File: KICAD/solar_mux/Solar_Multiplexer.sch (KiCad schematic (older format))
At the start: 34 parts, among them J1 Conn_01x14, J2 Conn_02x06_Odd_Even, J3 Conn_02x06_Odd_Even, U1 ASSR-1611, U10 ASSR-1611, U11 ASSR-1611, U12 ASSR-1611, U13 ASSR-1611, U14 ASSR-1611, U15 ASSR-1611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

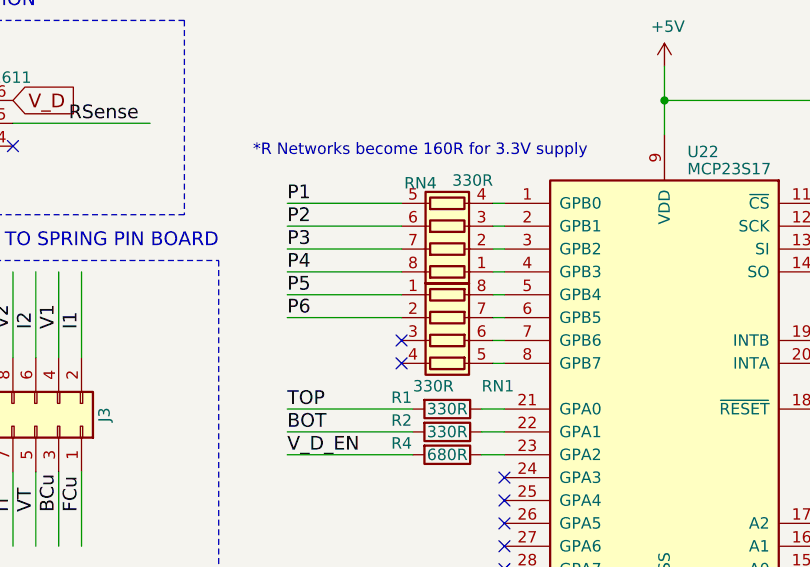
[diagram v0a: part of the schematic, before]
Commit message: Changing Via sizes and track widths
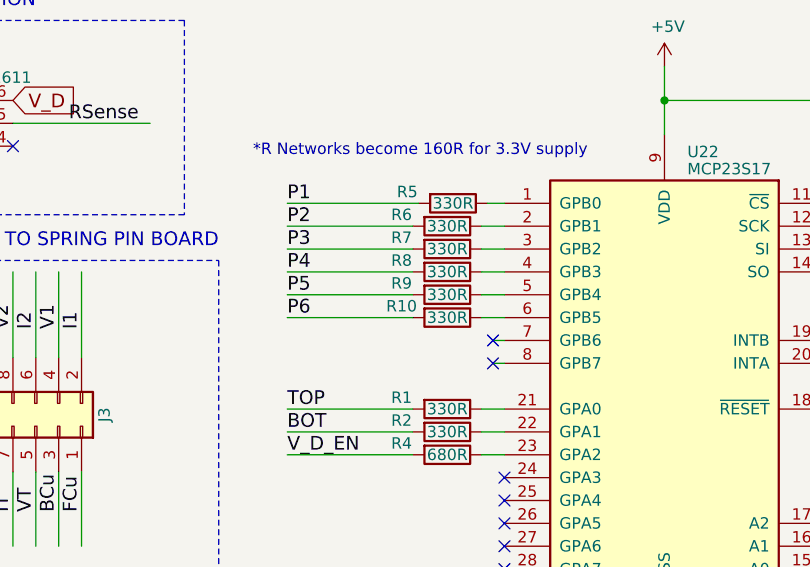
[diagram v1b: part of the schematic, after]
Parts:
- removed RN1, RN4: 330R, Resistor_SMD:R_Array_Convex_4x1206, symbol Device:R_Pack04
- added R10, R5, R6, R7, R8, R9: 330R, Resistor_THT:R_Axial_DIN0309_L9.0mm_D3.2mm_P15.24mm_Horizontal, symbol Device:R
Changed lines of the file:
@@
 	8500 2050 8450 2050
-Wire Wire Line
-	8500 1950 8450 1950
-Wire Wire Line
-	8500 1850 8450 1850
-Wire Wire Line
-	8500 1750 8450 1750
-Wire Wire Line
-	8500 1650 8450 1650
-Wire Wire Line
-	8500 1550 8450 1550
-Wire Wire Line
-	8500 1450 8450 1450
 Wire Wire Line
 	2150 1400 3750 1400
@@
 $EndComp
 $Comp
-L Device:R_Pack04 RN4
-U 1 1 5A00668D
-P 8250 1550
-F 0 "RN4" V 8438 1596 50  0000 L CNN
-F 1 "330R" V 8450 1350 50  0000 L CNN
-F 2 "Resistor_SMD:R_Array_Convex_4x1206" V 8525 1550 50  0001 C CNN
-F 3 "" H 8250 1550 50  0001 C CNN
-F 4 "744C083331JPCT-ND" H 8250 1550 60  0001 C CNN "digikey"
-	1    8250 1550
-	0    -1   -1   0
-$EndComp
-$Comp
 L Connector:TestPoint TP1
 U 1 1 5A007B84
@@
 	1    0    0    -1
 $EndComp
-$Comp
-L Device:R_Pack04 RN1
-U 1 1 5C453849
-P 8250 2050
-F 0 "RN1" V 8450 2200 50  0000 L CNN
-F 1 "330R" V 8450 1900 50  0000 L CNN
-F 2 "Resistor_SMD:R_Array_Convex_4x1206" V 8525 2050 50  0001 C CNN
-F 3 "" H 8250 2050 50  0001 C CNN
-F 4 "744C083331JPCT-ND" H 8250 2050 60  0001 C CNN "digikey"
-	1    8250 2050
-	0    1    1    0
-$EndComp
 Wire Wire Line
 	2200 4200 2150 4200
@@
 Text Label 6450 2000 1    60   ~ 0
 I2
-NoConn ~ 8050 2050
-NoConn ~ 8050 2150
+NoConn ~ 8450 2050
+NoConn ~ 8450 2150
 $Comp
 L power:+5V #PWR0107
@@
 	1    0    0    -1
 $EndComp
-Wire Wire Line
-	7550 1450 8050 1450
-Wire Wire Line
-	7550 1550 8050 1550
-Wire Wire Line
-	7550 1650 8050 1650
-Wire Wire Line
-	7550 1750 8050 1750
-Wire Wire Line
-	7550 1850 8050 1850
-Wire Wire Line
-	7550 1950 8050 1950
+$Comp
+L Device:R R5
+U 1 1 60480F1E
+P 8275 1450
+F 0 "R5" V 8225 1250 50  0000 C CNN
+F 1 "330R" V 8275 1450 50  0000 C CNN
+F 2 "Resistor_THT:R_Axial_DIN0309_L9.0mm_D3.2mm_P15.24mm_Horizontal" V 8205 1450 50  0001 C CNN
+F 3 "" H 8275 1450 50  0000 C CNN
+F 4 "2073607" H -2325 450 50  0001 C CNN "farnellCode"
+	1    8275 1450
+	0    1    1    0
+$EndComp
+Wire Wire Line
+	8425 1450 8500 1450
+Wire Wire Line
+	7550 1450 8125 1450
+$Comp
+L Device:R R6
+U 1 1 60492A33
+P 8250 1550
+F 0 "R6" V 8200 1350 50  0000 C CNN
+F 1 "330R" V 8250 1550 50  0000 C CNN
+F 2 "Resistor_THT:R_Axial_DIN0309_L9.0mm_D3.2mm_P15.24mm_Horizontal" V 8180 1550 50  0001 C CNN
+F 3 "" H 8250 1550 50  0000 C CNN
+F 4 "2073607" H -2350 550 50  0001 C CNN "farnellCode"
+	1    8250 1550
+	0    1    1    0
+$EndComp
+Wire Wire Line
+	7550 1550 8100 1550
+Wire Wire Line
+	8400 1550 8500 1550
+$Comp
+L Device:R R7
+U 1 1 604A1B89
+P 8250 1650
+F 0 "R7" V 8200 1450 50  0000 C CNN
+F 1 "330R" V 8250 1650 50  0000 C CNN
+F 2 "Resistor_THT:R_Axial_DIN0309_L9.0mm_D3.2mm_P15.24mm_Horizontal" V 8180 1650 50  0001 C CNN
+F 3 "" H 8250 1650 50  0000 C CNN
+F 4 "2073607" H -2350 650 50  0001 C CNN "farnellCode"
+	1    8250 1650
+	0    1    1    0
+$EndComp
+Wire Wire Line
+	7550 1650 8100 1650
+Wire Wire Line
+	8400 1650 8500 1650
+$Comp
+L Device:R R8
+U 1 1 604B1522
+P 8250 1750
+F 0 "R8" V 8200 1550 50  0000 C CNN
+F 1 "330R" V 8250 1750 50  0000 C CNN
+F 2 "Resistor_THT:R_Axial_DIN0309_L9.0mm_D3.2mm_P15.24mm_Horizontal" V 8180 1750 50  0001 C CNN
+F 3 "" H 8250 1750 50  0000 C CNN
+F 4 "2073607" H -2350 750 50  0001 C CNN "farnellCode"
+	1    8250 1750
+	0    1    1    0
+$EndComp
+Wire Wire Line
+	7550 1750 8100 1750
+Wire Wire Line
+	8400 1750 8500 1750
+$Comp
+L Device:R R9
+U 1 1 604C0378
+P 8250 1850
+F 0 "R9" V 8200 1650 50  0000 C CNN
+F 1 "330R" V 8250 1850 50  0000 C CNN
+F 2 "Resistor_THT:R_Axial_DIN0309_L9.0mm_D3.2mm_P15.24mm_Horizontal" V 8180 1850 50  0001 C CNN
+F 3 "" H 8250 1850 50  0000 C CNN
+F 4 "2073607" H -2350 850 50  0001 C CNN "farnellCode"
+	1    8250 1850
+	0    1    1    0
+$EndComp
+Wire Wire Line
+	7550 1850 8100 1850
+Wire Wire Line
+	8400 1850 8500 1850
+$Comp
+L Device:R R10
+U 1 1 604CF01C
+P 8250 1950
+F 0 "R10" V 8200 1750 50  0000 C CNN
+F 1 "330R" V 8250 1950 50  0000 C CNN
+F 2 "Resistor_THT:R_Axial_DIN0309_L9.0mm_D3.2mm_P15.24mm_Horizontal" V 8180 1950 50  0001 C CNN
+F 3 "" H 8250 1950 50  0000 C CNN
+F 4 "2073607" H -2350 950 50  0001 C CNN "farnellCode"
+	1    8250 1950
+	0    1    1    0
+$EndComp
+Wire Wire Line
+	7550 1950 8100 1950
+Wire Wire Line
+	8400 1950 8500 1950
 $EndSCHEMATC
